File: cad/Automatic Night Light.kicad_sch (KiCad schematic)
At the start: 11 parts, among them Q1 2N3904, SW1 SW_Push

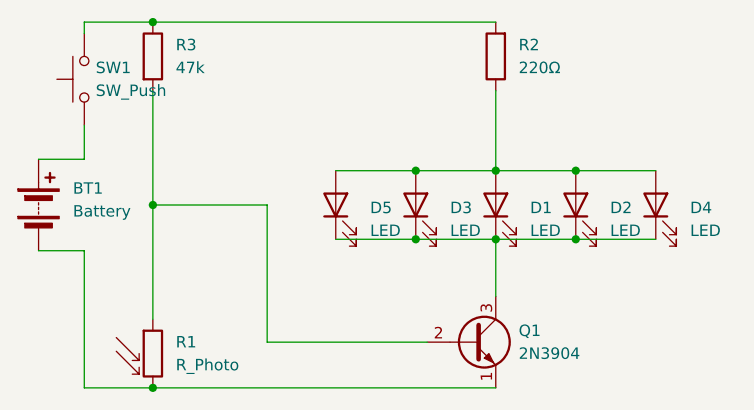
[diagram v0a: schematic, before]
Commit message: Add separate resistors for LEDs
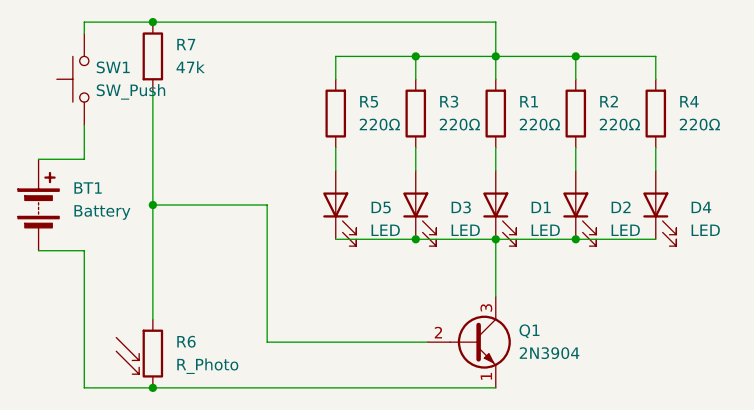
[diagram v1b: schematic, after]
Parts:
- added R2, R3, R4, R5: 220Ω, Resistor_THT:R_Axial_DIN0207_L6.3mm_D2.5mm_P7.62mm_Horizontal, symbol Device:R
- renumbered R2 to R1, R1 to R6, R3 to R7
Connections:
- net at R1.2, R7.1, SW1.2: now also R2.2, R3.2, R4.2, R5.2
- new net: D3.2 (A), R3.1
- new net: D4.2 (A), R4.1
- new net: D5.2 (A), R5.1
- new net: D2.2 (A), R2.1
- new net: D1.2 (A), R1.1
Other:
- moved on the sheet: R1
